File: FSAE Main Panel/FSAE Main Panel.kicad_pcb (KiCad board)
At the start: 2 copper layers, 0 parts

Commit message: LED Layout
LED placement and initial routing
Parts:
- added C101: 10uF, Capacitors_SMD:C_1206, F.Cu at (194.9, 193.1)
- added C102: 0.1uF, Capacitors_SMD:C_0603, F.Cu at (205.6, 189.2)
- added C103: 9.1pF, Capacitors_SMD:C_0402_NoSilk, F.Cu at (212.9, 188.1)
- added C104: 9.1pF, Capacitors_SMD:C_0402_NoSilk, F.Cu at (210.7, 191.3)
- added C105: 0.1uF, Capacitors_SMD:C_0603, F.Cu at (209.4, 189.2)
- added C106: 0.1uF, Capacitors_SMD:C_0603, F.Cu at (207.3, 191.5)
- added C107: 0.1uF, Capacitors_SMD:C_0603, F.Cu at (203.4, 192.7)
- added C108: 0.1uF, Capacitors_SMD:C_0603, F.Cu at (199.6, 192.7)
- added C109: 1uF, Capacitors_SMD:C_0603, F.Cu at (212.6, 186.0)
- added C110: 9.1pF, Capacitors_SMD:C_0402_NoSilk, F.Cu at (216.1, 185.7)
- added C111: 9.1pF, Capacitors_SMD:C_0402_NoSilk, F.Cu at (206.9, 193.6)
- added C201: 1uF, Capacitors_SMD:C_0603, F.Cu at (162.5, 203.4)
- added C202: 1uF, Capacitors_SMD:C_0603, F.Cu at (141.6, 212.2)
- added C203: 4700pF, Capacitors_SMD:C_0603, F.Cu at (182.3, 187.8)
- added C204: 4700pF, Capacitors_SMD:C_0603, F.Cu at (166.3, 203.4)
- added C205: 0.1uF, Capacitors_SMD:C_0603, F.Cu at (161.2, 205.7)
- added C206: 0.1uF, Capacitors_SMD:C_0603, F.Cu at (153.2, 213.9)
- added C207: 0.1uF, Capacitors_SMD:C_0603, F.Cu at (145.5, 213.9)
- added C208: 0.1uF, Capacitors_SMD:C_0603, F.Cu at (187.2, 183.5)
- added C209: 0.1uF, Capacitors_SMD:C_0603, F.Cu at (149.3, 213.9)
- added C210: 0.1uF, Capacitors_SMD:C_0603, F.Cu at (153.5, 210.3)
- added C211: 0.1uF, Capacitors_SMD:C_0603, F.Cu at (157.3, 207.9)
- added C212: 1uF, Capacitors_SMD:C_0603, F.Cu at (187.2, 181.1)
- added C213: 4700pF, Capacitors_SMD:C_0603, F.Cu at (153.5, 207.9)
- added C214: 0.1uF, Capacitors_SMD:C_0603, F.Cu at (157.3, 210.3)
- added C215: 1uF, Capacitors_SMD:C_0603, F.Cu at (157.0, 212.6)
- added C216: 4700pF, Capacitors_SMD:C_0603, F.Cu at (158.6, 203.4)
- added C301: 22uF, Capacitors_THT:CP_Radial_D5.0mm_P2.00mm, F.Cu at (215.0, 149.1)
- added C302: 2.2uF, Capacitors_SMD:C_1206, F.Cu at (215.7, 163.0)
- added C303: 4700pF, Capacitors_SMD:C_0603, F.Cu at (232.1, 153.9)
- added C304: 2.2uF, Capacitors_SMD:C_1206, F.Cu at (236.4, 143.8)
- added C305: 0.1uF, Capacitors_SMD:C_0603, F.Cu at (237.7, 151.6)
- added C306: 2.2uF, Capacitors_SMD:C_1206, F.Cu at (216.1, 159.6)
- added C307: 22uF, Capacitors_THT:CP_Radial_D5.0mm_P2.00mm, B.Cu at (269.7, 95.2)
- added C308: 100uF, Capacitors_THT:CP_Radial_D5.0mm_P2.00mm, B.Cu at (269.7, 88.1)
- added C309: 22uF, Capacitors_THT:CP_Radial_D5.0mm_P2.00mm, F.Cu at (222.1, 149.1)
- added C310: 2.2uF, Capacitors_SMD:C_1206, F.Cu at (222.5, 154.1)
- added C311: 22uF, Capacitors_THT:CP_Radial_D5.0mm_P2.00mm, F.Cu at (208.9, 158.0)
- added C312: 100uF, Capacitors_THT:CP_Radial_D5.0mm_P2.00mm, F.Cu at (229.2, 142.4)
- added C313: 10uF, Capacitors_SMD:C_1206, F.Cu at (221.6, 159.6)
- added C314: 1uF, Capacitors_SMD:C_0603, F.Cu at (226.3, 160.7)
- added C315: 0.1uF, Capacitors_SMD:C_0603, F.Cu at (238.8, 146.5)
- added C316: 0.1uF, Capacitors_SMD:C_0603, F.Cu at (203.8, 164.1)
- added C317: 1uF, Capacitors_SMD:C_0603, F.Cu at (233.9, 151.6)
- added C318: 10uF, Capacitors_SMD:C_1206, F.Cu at (199.1, 164.5)
- added C319: 1uF, Capacitors_SMD:C_0603, F.Cu at (230.2, 158.3)
- added C320: 1uF, Capacitors_SMD:C_0603, F.Cu at (226.3, 158.3)
- added C321: 10uF, Capacitors_SMD:C_1206, F.Cu at (229.2, 147.4)
- added C322: 1uF, Capacitors_SMD:C_0603, F.Cu at (238.8, 148.9)
- added C323: 1uF, Capacitors_SMD:C_0603, F.Cu at (242.6, 144.8)
- added C324: 10uF, Capacitors_SMD:C_1206, F.Cu at (236.4, 140.6)
- added C401: 1uF, Capacitors_SMD:C_0603, F.Cu at (204.2, 209.4)
- added C402: 0.1uF, Capacitors_SMD:C_0603, F.Cu at (214.7, 198.9)
- added C403: 0.1uF, Capacitors_SMD:C_0603, F.Cu at (210.8, 201.2)
- added C404: 1uF, Capacitors_SMD:C_0603, F.Cu at (209.6, 203.7)
- added C405: 0.1uF, Capacitors_SMD:C_0603, F.Cu at (210.8, 198.9)
- added C406: 0.1uF, Capacitors_SMD:C_0603, F.Cu at (204.2, 207.1)
- added C407: 9.1pF, Capacitors_SMD:C_0402_NoSilk, F.Cu at (214.7, 205.8)
- added C408: 9.1pF, Capacitors_SMD:C_0402_NoSilk, F.Cu at (214.3, 201.0)
- added C501: 1uF, Capacitors_SMD:C_0603, F.Cu at (188.1, 142.5)
- added C502: 0.1uF, Capacitors_SMD:C_0603, F.Cu at (179.1, 150.8)
- added C504: 0.1uF, Capacitors_SMD:C_0603, F.Cu at (153.3, 175.2)
- added C505: 0.1uF, Capacitors_SMD:C_0603, F.Cu at (188.1, 140.2)
- added C506: 1uF, Capacitors_SMD:C_0603, F.Cu at (157.7, 170.7)
- added C507: 1uF, Capacitors_SMD:C_0603, F.Cu at (173.8, 153.4)
- added D201: PRTR5V0U2X, TO_SOT_Packages_SMD:SOT-143, F.Cu at (154.1, 204.5)
- added D301: D, Diodes_SMD:D_SOD-123F, F.Cu at (229.2, 150.6)
- added D302: D_TVS, Resistors_SMD:R_0603, F.Cu at (230.0, 160.8)
- added D401: D, Diodes_SMD:D_SOD-123F, F.Cu at (205.0, 204.2)
- added D502: SM1206NPGC-IL, LEDs:LED_1206, F.Cu at (125.0, 69.0)
- added D503: SM1206NPGC-IL, LEDs:LED_1206, F.Cu at (129.0, 69.0)
- added D504: SM1206NPGC-IL, LEDs:LED_1206, F.Cu at (133.0, 69.0)
- added D505: SM1206NPGC-IL, LEDs:LED_1206, F.Cu at (137.0, 69.0)
- added D506: SM1206NPGC-IL, LEDs:LED_1206, F.Cu at (141.0, 69.0)
- added D507: SM1206NPGC-IL, LEDs:LED_1206, F.Cu at (145.0, 69.0)
- added D508: SM1206NPGC-IL, LEDs:LED_1206, F.Cu at (149.0, 69.0)
- added D509: SM1206NPGC-IL, LEDs:LED_1206, F.Cu at (153.0, 69.0)
- added D510: SM1206NPGC-IL, LEDs:LED_1206, F.Cu at (157.0, 69.0)
- added D511: SM1206NPGC-IL, LEDs:LED_1206, F.Cu at (161.0, 69.0)
- added D512: SM1206NPGC-IL, LEDs:LED_1206, F.Cu at (165.0, 69.0)
- added D513: SM1206NPGC-IL, LEDs:LED_1206, F.Cu at (169.0, 69.0)
- added D514: SM1206NPGC-IL, LEDs:LED_1206, F.Cu at (173.0, 69.0)
- added D515: SM1206NPGC-IL, LEDs:LED_1206, F.Cu at (177.0, 69.0)
- added D516: SM1206NPGC-IL, LEDs:LED_1206, F.Cu at (181.0, 69.0)
- added D517: SM1206NPGC-IL, LEDs:LED_1206, F.Cu at (185.0, 69.0)
- added D518: SM1206NYC-IL, LEDs:LED_1206, F.Cu at (189.0, 69.0)
- added D519: SM1206NYC-IL, LEDs:LED_1206, F.Cu at (193.0, 69.0)
- added D520: SM1206NYC-IL, LEDs:LED_1206, F.Cu at (197.0, 69.0)
- added D521: SM1206NYC-IL, LEDs:LED_1206, F.Cu at (201.0, 69.0)
- added D522: SM1206NYC-IL, LEDs:LED_1206, F.Cu at (205.0, 69.0)
- added D523: SM1206NYC-IL, LEDs:LED_1206, F.Cu at (209.0, 69.0)
- added D524: SM1206NYC-IL, LEDs:LED_1206, F.Cu at (213.0, 69.0)
- added D525: SM1206NYC-IL, LEDs:LED_1206, F.Cu at (217.0, 69.0)
- added D526: SM1206NHC-IL, LEDs:LED_1206, F.Cu at (221.0, 69.0)
- added D527: SM1206NHC-IL, LEDs:LED_1206, F.Cu at (225.0, 69.0)
- added D528: SM1206NHC-IL, LEDs:LED_1206, F.Cu at (229.0, 69.0)
- added D529: SM1206NHC-IL, LEDs:LED_1206, F.Cu at (233.0, 69.0)
- added D530: SM1206NHC-IL, LEDs:LED_1206, F.Cu at (237.0, 69.0)
- added D531: SM1206NHC-IL, LEDs:LED_1206, F.Cu at (241.0, 69.0)
- added D532: SM1206NHC-IL, LEDs:LED_1206, F.Cu at (117.5, 223.6)
- added D533: SM1206NHC-IL, LEDs:LED_1206, F.Cu at (120.5, 223.6)
- added D534: LCB G6SP-DBFA-4J5L-0-140-R18-Z, FSAE2020:LCB_G6SP, F.Cu at (112.0, 70.4)
- added D535: LCB G6SP-DBFA-4J5L-0-140-R18-Z, FSAE2020:LCB_G6SP, F.Cu at (119.0, 70.5)
- added D536: LCB G6SP-DBFA-4J5L-0-140-R18-Z, FSAE2020:LCB_G6SP, F.Cu at (254.0, 70.5)
- added D537: LCB G6SP-DBFA-4J5L-0-140-R18-Z, FSAE2020:LCB_G6SP, F.Cu at (247.0, 70.5)
- added D538: SM1206NUWC-IL, LEDs:LED_1206, F.Cu at (185.0, 87.0)
- added D539: SM1206NUWC-IL, LEDs:LED_1206, F.Cu at (190.0, 92.0)
- added D540: SM1206NUWC-IL, LEDs:LED_1206, F.Cu at (188.0, 102.0)
- added D541: SM1206NUWC-IL, LEDs:LED_1206, F.Cu at (181.0, 107.0)
- added D542: SM1206NUWC-IL, LEDs:LED_1206, F.Cu at (176.0, 102.0)
- added D543: SM1206NUWC-IL, LEDs:LED_1206, F.Cu at (178.0, 92.0)
- added D544: SM1206NUWC-IL, LEDs:LED_1206, F.Cu at (183.0, 97.0)
- added D550: SM1206NYC-IL, LEDs:LED_1206, F.Cu at (131.7, 97.5)
- added D551: SM1206NYC-IL, LEDs:LED_1206, F.Cu at (128.7, 95.7)
- added D552: SM1206NYC-IL, LEDs:LED_1206, F.Cu at (128.7, 92.2)
- added D553: SM1206NYC-IL, LEDs:LED_1206, F.Cu at (131.7, 90.5)
- added D554: SM1206NYC-IL, LEDs:LED_1206, F.Cu at (134.7, 92.2)
- added D555: SM1206NYC-IL, LEDs:LED_1206, F.Cu at (134.7, 95.7)
- added D556: SM1206NHC-IL, LEDs:LED_1206, F.Cu at (234.0, 97.5)
- added D557: SM1206NHC-IL, LEDs:LED_1206, F.Cu at (231.0, 95.7)
- added D557: SM1206NHC-IL, LEDs:LED_1206, F.Cu at (143.3, 155.4)
- added D558: SM1206NHC-IL, LEDs:LED_1206, F.Cu at (231.0, 92.2)
- added D558: SM1206NHC-IL, LEDs:LED_1206, F.Cu at (149.6, 149.3)
- added D559: SM1206NHC-IL, LEDs:LED_1206, F.Cu at (234.1, 90.5)
- added D559: SM1206NHC-IL, LEDs:LED_1206, F.Cu at (135.1, 164.7)
- added D560: SM1206NHC-IL, LEDs:LED_1206, F.Cu at (237.1, 92.3)
- added D560: SM1206NHC-IL, LEDs:LED_1206, F.Cu at (143.3, 152.3)
- added D561: SM1206NHC-IL, LEDs:LED_1206, F.Cu at (237.1, 95.8)
- added D561: SM1206NHC-IL, LEDs:LED_1206, F.Cu at (152.2, 143.6)
- added F201: MF-MSMF050-2, MF-MSMF050-2:MF-MSMF050-2, F.Cu at (136.3, 213.1)
- added F301: MF-MSMF050-2, MF-MSMF050-2:MF-MSMF050-2, F.Cu at (209.5, 163.5)
- added J1: Conn_01x08, Connectors_Molex:Molex_KK-6410-08_08x2.54mm_Straight, B.Cu at (270.5, 105.6)
- added J2: Conn_01x08, Connectors_Molex:Molex_KK-6410-08_08x2.54mm_Straight, B.Cu at (102.6, 96.7)
- added J3: Conn_01x10, Connectors_Molex:Molex_KK-6410-10_10x2.54mm_Straight, B.Cu at (108.8, 143.0)
- added J4: USB Micro B, 10118192-0001LF:10118192-0001LF, B.Cu at (202.6, 123.3)
- added J5: Cortex_Debug, Pin_Headers:Pin_Header_Straight_2x05_Pitch1.27mm, F.Cu at (205.6, 110.3)
- added J6: Conn_01x08, Connectors_Molex:Molex_KK-6410-08_08x2.54mm_Straight, B.Cu at (126.0, 129.5)
- added L101: BLM41PG471SN1L, Inductors_SMD:L_1806, F.Cu at (207.2, 186.3)
- added L201: BLM41PG471SN1L, Inductors_SMD:L_1806, F.Cu at (129.5, 212.1)
- added L301: 1.8uH, FSAE2020:SRP1238A, B.Cu at (256.1, 99.3)
- added Q301: IRLML6402TRPBF, TO_SOT_Packages_SMD:SOT-23, F.Cu at (220.7, 163.4)
- added Q501: SI2308CDS-T1-GE3, TO_SOT_Packages_SMD:SOT-23, F.Cu at (242.5, 81.4)
- added Q502: SI2308CDS-T1-GE3, TO_SOT_Packages_SMD:SOT-23, F.Cu at (153.6, 171.8)
- added Q503: SI2308CDS-T1-GE3, TO_SOT_Packages_SMD:SOT-23, F.Cu at (123.0, 80.5)
- added Q504: SI2308CDS-T1-GE3, TO_SOT_Packages_SMD:SOT-23, F.Cu at (167.7, 160.6)
- added R201: 10k, Resistors_SMD:R_0603, F.Cu at (168.4, 205.9)
- added R202: 330, Resistors_SMD:R_0603, F.Cu at (161.0, 208.1)
- added R203: 10k, Resistors_SMD:R_0603, F.Cu at (182.2, 195.1)
- added R204: 330, Resistors_SMD:R_0603, F.Cu at (173.6, 203.4)
- added R205: 10k, Resistors_SMD:R_0603, F.Cu at (172.0, 205.9)
- added R206: 330, Resistors_SMD:R_0603, F.Cu at (164.3, 213.2)
- added R207: 10k, Resistors_SMD:R_0603, F.Cu at (185.7, 190.3)
- added R208: 330, Resistors_SMD:R_0603, F.Cu at (171.7, 208.4)
- added R209: 10k, Resistors_SMD:R_0603, F.Cu at (168.1, 210.9)
- added R210: 330, Resistors_SMD:R_0603, F.Cu at (185.7, 192.8)
- added R211: 10k, Resistors_SMD:R_0603, F.Cu at (168.1, 208.4)
- added R212: 330, Resistors_SMD:R_0603, F.Cu at (161.0, 210.6)
- added R213: 10k, Resistors_SMD:R_0603, F.Cu at (164.9, 205.8)
- added R214: 330, Resistors_SMD:R_0603, F.Cu at (182.2, 190.2)
- added R215: 10k, Resistors_SMD:R_0603, F.Cu at (186.0, 187.8)
- added R216: 330, Resistors_SMD:R_0603, F.Cu at (164.6, 208.3)
- added R217: 1M, Resistors_SMD:R_0603, F.Cu at (170.0, 203.4)
- added R218: 10k, Resistors_SMD:R_0603, F.Cu at (160.7, 213.1)
- added R219: 1M, Resistors_SMD:R_0603, F.Cu at (182.2, 192.7)
- added R220: 1k, Resistors_SMD:R_0603, F.Cu at (164.6, 210.7)
- added R301: 41.2k, Resistors_SMD:R_0603, F.Cu at (242.5, 147.3)
- added R302: 100m, Resistors_SMD:R_0603, F.Cu at (224.7, 163.1)
- added R303: 1k, Resistors_SMD:R_0603, F.Cu at (235.8, 154.0)
- added R304: 301k, Resistors_SMD:R_0603, F.Cu at (233.9, 156.5)
- added R305: 100k, Resistors_SMD:R_0603, F.Cu at (242.5, 149.7)
- added R306: 86.6k, Resistors_SMD:R_0603, F.Cu at (228.2, 163.2)
- added R307: 11.8k, Resistors_SMD:R_0603, F.Cu at (233.9, 159.0)
- added R401: 120, Resistors_SMD:R_0603, F.Cu at (207.9, 207.2)
- added R402: 1k, Resistors_SMD:R_0603, F.Cu at (213.3, 203.7)
- added R403: 10k, Resistors_SMD:R_0603, F.Cu at (207.9, 209.6)
- added R404: 10k, Resistors_SMD:R_0603, F.Cu at (211.4, 206.2)
- added R405: 0, Resistors_SMD:R_0603, F.Cu at (211.4, 208.6)
- added R502: 120, Resistors_SMD:R_0603, F.Cu at (125.0, 75.0)
- added R503: 120, Resistors_SMD:R_0603, F.Cu at (129.0, 75.0)
- added R504: 120, Resistors_SMD:R_0603, F.Cu at (133.0, 75.0)
- added R505: 120, Resistors_SMD:R_0603, F.Cu at (137.0, 75.0)
- added R506: 120, Resistors_SMD:R_0603, F.Cu at (141.0, 75.0)
- added R507: 120, Resistors_SMD:R_0603, F.Cu at (145.0, 75.0)
- added R508: 120, Resistors_SMD:R_0603, F.Cu at (149.0, 75.0)
- added R509: 120, Resistors_SMD:R_0603, F.Cu at (153.0, 75.0)
- added R510: 120, Resistors_SMD:R_0603, F.Cu at (157.0, 75.0)
- added R511: 120, Resistors_SMD:R_0603, F.Cu at (161.0, 75.0)
- added R512: 120, Resistors_SMD:R_0603, F.Cu at (165.0, 75.0)
- added R513: 120, Resistors_SMD:R_0603, F.Cu at (169.0, 75.0)
- added R514: 120, Resistors_SMD:R_0603, F.Cu at (173.0, 75.0)
- added R515: 120, Resistors_SMD:R_0603, F.Cu at (177.0, 75.0)
- added R516: 120, Resistors_SMD:R_0603, F.Cu at (181.0, 75.0)
- added R517: 120, Resistors_SMD:R_0603, F.Cu at (185.0, 75.0)
- added R518: 120, Resistors_SMD:R_0603, F.Cu at (189.0, 75.0)
- added R519: 120, Resistors_SMD:R_0603, F.Cu at (193.0, 75.0)
- added R520: 120, Resistors_SMD:R_0603, F.Cu at (197.0, 75.0)
- added R521: 120, Resistors_SMD:R_0603, F.Cu at (201.0, 75.0)
- added R522: 120, Resistors_SMD:R_0603, F.Cu at (205.0, 75.0)
- added R523: 120, Resistors_SMD:R_0603, F.Cu at (209.0, 75.0)
- added R524: 120, Resistors_SMD:R_0603, F.Cu at (213.0, 75.0)
- added R525: 120, Resistors_SMD:R_0603, F.Cu at (217.0, 75.0)
- added R526: 120, Resistors_SMD:R_0603, F.Cu at (221.0, 75.0)
- added R527: 120, Resistors_SMD:R_0603, F.Cu at (225.0, 75.0)
- added R528: 120, Resistors_SMD:R_0603, F.Cu at (229.0, 75.0)
- added R529: 120, Resistors_SMD:R_0603, F.Cu at (233.0, 75.0)
- added R530: 120, Resistors_SMD:R_0603, F.Cu at (237.0, 75.0)
- added R531: 120, Resistors_SMD:R_0603, F.Cu at (241.0, 75.0)
- added R532: 120, Resistors_SMD:R_0603, F.Cu at (157.0, 175.6)
- added R533: 120, Resistors_SMD:R_0603, F.Cu at (167.5, 164.1)
- added R534: 11, Resistors_SMD:R_1210, F.Cu at (112.0, 76.0)
- added R535: 11, Resistors_SMD:R_1210, F.Cu at (119.0, 76.0)
- added R536: 11, Resistors_SMD:R_1210, F.Cu at (254.0, 76.0)
- added R537: 11, Resistors_SMD:R_1210, F.Cu at (247.0, 76.0)
- added R550: 120, Resistors_SMD:R_0603, F.Cu at (128.1, 99.3)
- added R551: 120, Resistors_SMD:R_0603, F.Cu at (125.3, 93.6)
- added R551: 120, Resistors_SMD:R_0603, F.Cu at (165.0, 171.6)
- added R552: 120, Resistors_SMD:R_0603, F.Cu at (128.8, 88.2)
- added R552: 120, Resistors_SMD:R_0603, F.Cu at (191.5, 145.0)
- added R553: 120, Resistors_SMD:R_0603, F.Cu at (135.3, 88.6)
- added R553: 120, Resistors_SMD:R_0603, F.Cu at (171.0, 166.6)
- added R554: 120, Resistors_SMD:R_0603, F.Cu at (138.1, 94.4)
- added R554: 120, Resistors_SMD:R_0603, F.Cu at (168.5, 169.1)
- added R555: 120, Resistors_SMD:R_0603, F.Cu at (134.6, 99.8)
- added R555: 120, Resistors_SMD:R_0603, F.Cu at (184.6, 153.4)
- added R556: 120, Resistors_SMD:R_0603, F.Cu at (230.3, 99.4)
- added R557: 120, Resistors_SMD:R_0603, F.Cu at (227.5, 93.4)
- added R557: 120, Resistors_SMD:R_0603, F.Cu at (179.7, 158.5)
- added R558: 120, Resistors_SMD:R_0603, F.Cu at (231.2, 88.0)
- added R558: 120, Resistors_SMD:R_0603, F.Cu at (191.5, 147.4)
- added R559: 120, Resistors_SMD:R_0603, F.Cu at (237.8, 88.6)
- added R559: 120, Resistors_SMD:R_0603, F.Cu at (164.1, 175.2)
- added R560: 120, Resistors_SMD:R_0603, F.Cu at (240.6, 94.5)
- added R560: 120, Resistors_SMD:R_0603, F.Cu at (183.3, 155.9)
- added R561: 120, Resistors_SMD:R_0603, F.Cu at (236.9, 99.9)
- added R561: 120, Resistors_SMD:R_0603, F.Cu at (189.9, 149.9)
- added R562: 120, Resistors_SMD:R_0603, F.Cu at (178.8, 160.9)
- added R563: 120, Resistors_SMD:R_0603, F.Cu at (183.3, 158.4)
- added R564: 120, Resistors_SMD:R_0603, F.Cu at (186.4, 149.9)
- added R565: 120, Resistors_SMD:R_0603, F.Cu at (174.6, 165.9)
- added R566: 120, Resistors_SMD:R_0603, F.Cu at (172.1, 169.1)
- added R567: 120, Resistors_SMD:R_0603, F.Cu at (188.1, 152.4)
- added R568: 120, Resistors_SMD:R_0603, F.Cu at (178.1, 163.4)
- added SW1: SW_SPST, FSAE2020:PTS125, F.Cu at (152.6, 112.8)
- added SW2: SW_SPST, FSAE2020:PTS125, F.Cu at (133.8, 112.9)
- added U101: SAMD21G18A-AU, Housings_QFP:TQFP-48_7x7mm_Pitch0.5mm, B.Cu at (220.5, 108.6)
- added U201: CD40106BPWR, Housings_SSOP:TSSOP-14_4.4x5mm_Pitch0.65mm, B.Cu at (123.7, 116.7)
- added U202: CD74HC238PWR, Housings_SSOP:TSSOP-16_4.4x5mm_Pitch0.65mm, B.Cu at (115.0, 107.2)
- added U301: TPS53513, Texas_Additions:VQFN-CLIP-28-4.5x3.5mm, F.Cu at (189.6, 202.2)
- added U302: LM2940IMP-5.0/NOPB, TO_SOT_Packages_SMD:SOT-223-3_TabPin2, B.Cu at (239.8, 111.2)
- added U303: LP5907MFX-3.3, TO_SOT_Packages_SMD:SOT-23-5, F.Cu at (227.7, 154.8)
- added U304: LP5907MFX-3.3, TO_SOT_Packages_SMD:SOT-23-5, F.Cu at (241.6, 141.3)
- added U305: LP5907MFX-3.3, TO_SOT_Packages_SMD:SOT-23-5, F.Cu at (234.4, 148.1)
- added U401: MCP25625, FSAE2020:SSOP-28_5.3x10.2mm_Pitch0.65mm, B.Cu at (225.5, 124.0)
- added U501: TLC6C598, Housings_SSOP:TSSOP-16_4.4x5mm_Pitch0.65mm, B.Cu at (198.0, 99.7)
- added U502: TLC6C5816, TLC6C5816:TLC6C5816, B.Cu at (155.0, 88.0)
- added U503: TLC6C5816, TLC6C5816:TLC6C5816, B.Cu at (215.0, 88.0)
- added Y101: 32.768kHz, MS1V-T1K:MS1V-T1K, F.Cu at (207.5, 182.2)
- added Y102: 16MHz, Crystals:Crystal_SMD_5032-4pin_5.0x3.2mm, F.Cu at (215.1, 182.4)
- added Y401: 16MHz, Crystals:Crystal_SMD_5032-4pin_5.0x3.2mm, F.Cu at (205.6, 200.1)
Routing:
- net LED_+5V: track 0.00 -> 136.6 mm, vias 0 -> 2
- net /Display/RPM_16: track 0.00 -> 36.6 mm, vias 0 -> 1
- net /Display/RPM_1: track 0.00 -> 36.1 mm, vias 0 -> 1
- net /Display/RPM_15: track 0.00 -> 32.7 mm, vias 0 -> 1
- net /Display/RPM_2: track 0.00 -> 32.1 mm, vias 0 -> 1
- net /Display/RPM_14: track 0.00 -> 28.7 mm, vias 0 -> 1
- net /Display/RPM_3: track 0.00 -> 28.4 mm, vias 0 -> 1
- net /Display/RPM_13: track 0.00 -> 24.9 mm, vias 0 -> 1
- net /Display/RPM_4: track 0.00 -> 24.5 mm, vias 0 -> 1
- net /Display/RPM_12: track 0.00 -> 20.9 mm, vias 0 -> 1
- net /Display/RPM_5: track 0.00 -> 20.4 mm, vias 0 -> 1
- net /Display/RPM_11: track 0.00 -> 17.1 mm, vias 0 -> 1
- net /Display/SFT_2: track 0.00 -> 16.9 mm
- net /Display/RPM_6: track 0.00 -> 16.5 mm, vias 0 -> 1
- net /Display/RPM_8: track 0.00 -> 15.1 mm, vias 0 -> 1
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- added copper zone on F.Cu, net LED_+5V

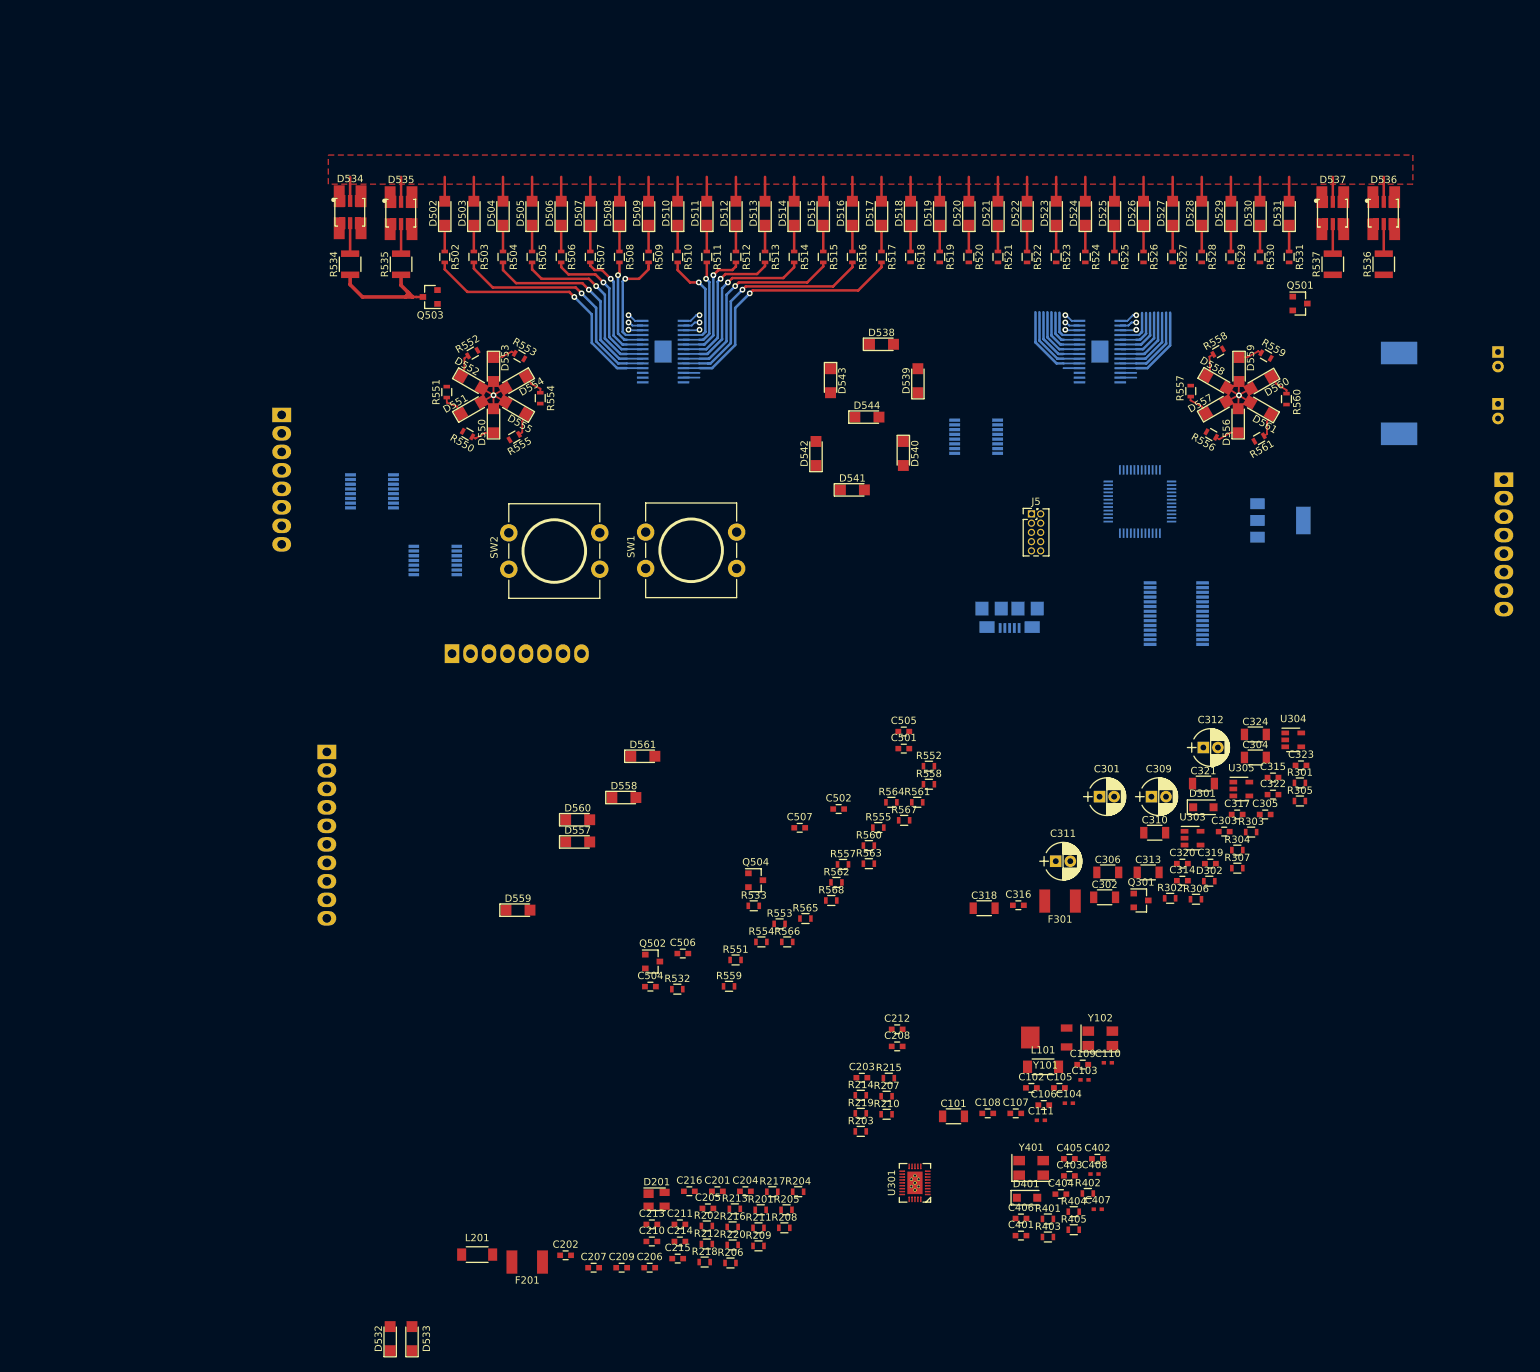
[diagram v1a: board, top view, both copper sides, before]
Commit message: Changed Display Power Reg
Swapped costly complex 5V Rail reg for smaller lower efficiency TPS564201
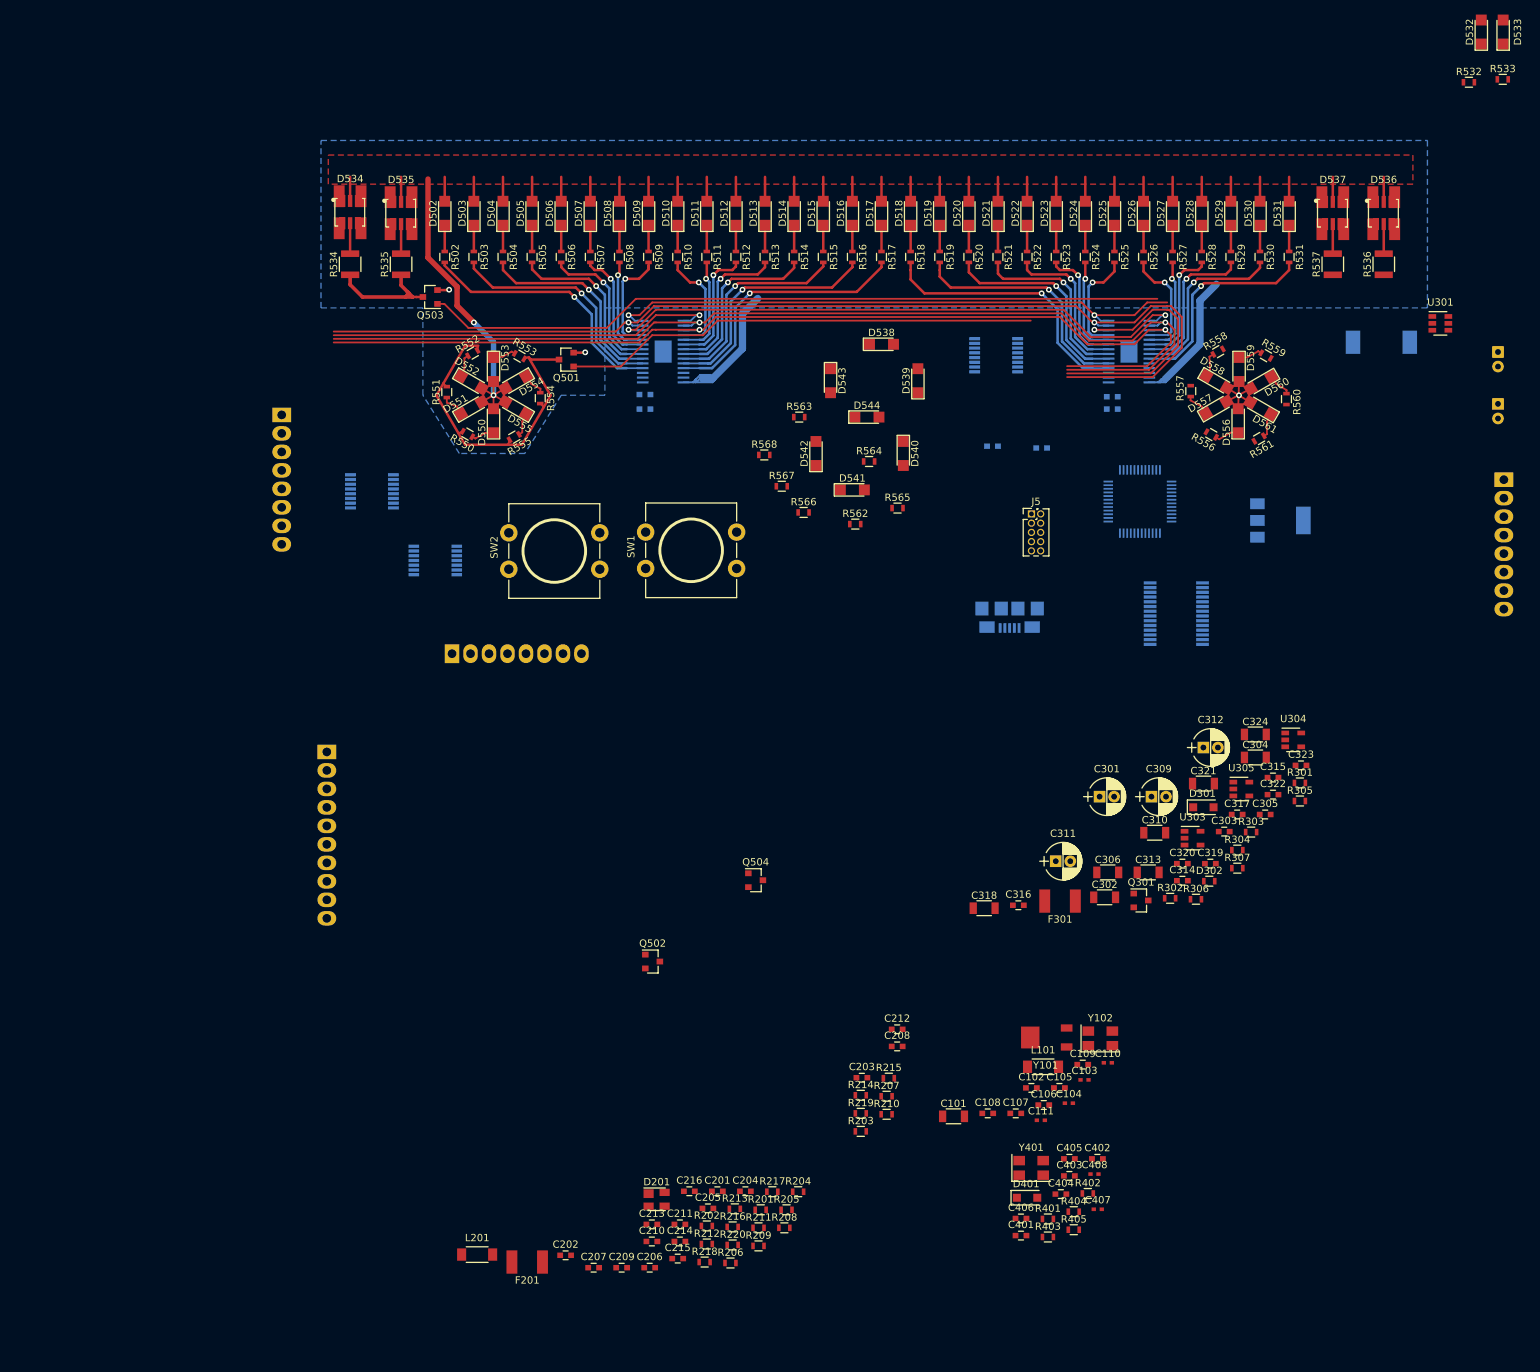
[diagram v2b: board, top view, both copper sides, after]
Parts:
- removed the D557 at (143.3, 155.4)
- removed the D558 at (149.6, 149.3)
- removed the D559 at (135.1, 164.7)
- removed the D560 at (143.3, 152.3)
- removed the D561 at (152.2, 143.6)
- removed the R551 at (165.0, 171.6)
- removed the R552 at (191.5, 145.0)
- removed the R553 at (171.0, 166.6)
- removed the R554 at (168.5, 169.1)
- removed the R555 at (184.6, 153.4)
- removed the R557 at (179.7, 158.5)
- removed the R558 at (191.5, 147.4)
- removed the R559 at (164.1, 175.2)
- removed the R560 at (183.3, 155.9)
- removed the R561 at (189.9, 149.9)
- C501, C502, C504, C505, C506, C507: moved to B.Cu
- L301: value 1.8uH -> 3.3uH; footprint FSAE2020:SRP1238A -> Inductors_SMD:L_Bourns-SRU8043
- R301: value 41.2k -> 56.2k
- R302: value 100m -> 10k
- U301: value TPS53513 -> TPS564201; footprint Texas_Additions:VQFN-CLIP-28-4.5x3.5mm -> TO_SOT_Packages_SMD:SOT-23-6
- moved D532 233.9 mm to (267.4, 44.1)
- moved D533 233.9 mm to (270.4, 44.1)
- moved R532 165.4 mm to (265.7, 51.0)
- moved R533 153.2 mm to (270.4, 50.6)
- moved U301 138.4 mm to (261.8, 84.1), turned to 0 degrees
- moved Q501 101.1 mm to (141.7, 89.1), turned to 180 degrees
- moved C504 81.3 mm to (152.5, 93.9), turned to 180 degrees
- moved C506 75.0 mm to (152.5, 95.9)
- moved C507 71.8 mm to (216.7, 95.9)
- moved R563 62.1 mm to (173.7, 97.0)
- moved R568 61.9 mm to (168.9, 102.2)
- moved R566 59.0 mm to (174.3, 110.1)
- moved R565 57.8 mm to (187.2, 109.5)
- moved C505 54.2 mm to (216.7, 94.2), turned to 180 degrees
- moved C502 54.1 mm to (200.2, 101.0)
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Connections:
- C305 pad 1: /Power/Vbst -> Net-(C305-Pad1)
- C305 pad 2: LED_+5V -> Net-(C305-Pad2)
- L301 pad 2: /Power/Vsw -> Net-(C305-Pad1)
- R301 pad 1: GND -> LED_+5V
- R301 pad 2: /Power/Vtrip -> Net-(R301-Pad2)
- R302 pad 1: /Power/Vreg -> Net-(R301-Pad2)
- R302 pad 2: /Power/Vmode -> GND
- U301 pad 1: /Power/Vrf -> GND
- U301 pad 2: PGOOD -> Net-(C305-Pad1)
- U301 pad 3: +5V -> CAN_V+
- U301 pad 4: /Power/Vbst -> Net-(R301-Pad2)
- U301 pad 5: Net-(U301-Pad5) -> CAN_V+
- U301 pad 6: /Power/Vsw -> Net-(C305-Pad2)
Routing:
- net FRAME_CLR: track 4.25 -> 146.3 mm
- net FRAME_SET: track 4.75 -> 142.9 mm
- net FRAME_CLK: track 4.46 -> 140.2 mm
- net SHIFT1: track 0.00 -> 101.9 mm
- net /Display/FRAME_INT2: track 4.71 -> 82.4 mm
- net ~RPM_EN: track 4.54 -> 80.7 mm
- net HIGH_TEMP: track 0.00 -> 65.4 mm
- net FRAME_OUT: track 2.62 -> 54.0 mm
- net GND: track 0.00 -> 48.6 mm, vias 0 -> 2
- net /Display/HT_CONTROL: track 0.00 -> 47.5 mm
- net /Display/RPM_17: track 2.20 -> 37.3 mm, vias 0 -> 1
- net /Display/FRAME_INT1: track 2.09 -> 35.8 mm
- net LED_+5V: track 136.6 -> 170.0 mm, vias 2 -> 3
- net /Display/RPM_18: track 11.4 -> 33.2 mm, vias 0 -> 1
- net /Display/RPM_19: track 10.4 -> 29.0 mm, vias 0 -> 1
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- added copper zone on B.Cu, net GND
